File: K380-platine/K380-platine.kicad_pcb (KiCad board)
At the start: 2 copper layers, 98 x 38 mm, 32 parts, among them J1 JST-PH 2, J2 Conn_01x23, J3 MicroMod-M.2E, J4 USB_C_Receptacle_USB2.0, J5 Conn_ARM_JTAG_SWD_10, Q1 PMost Enc FET -20V, Q2 Q_NMOS_DGS, SW1 EG1215AA, SW2 SW_Push, SW3 SW_Push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

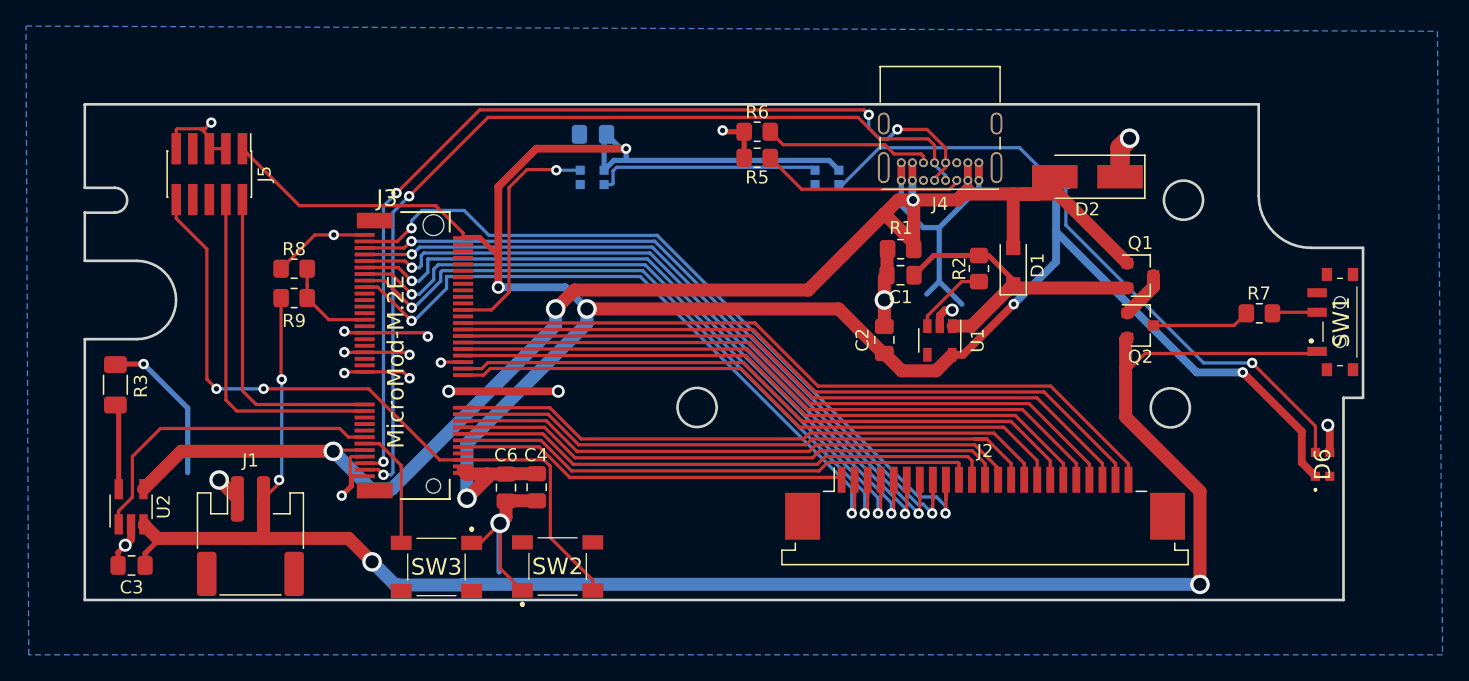
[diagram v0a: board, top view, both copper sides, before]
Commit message: Add drill mills
- needed to reroute a few tracks for it to fit
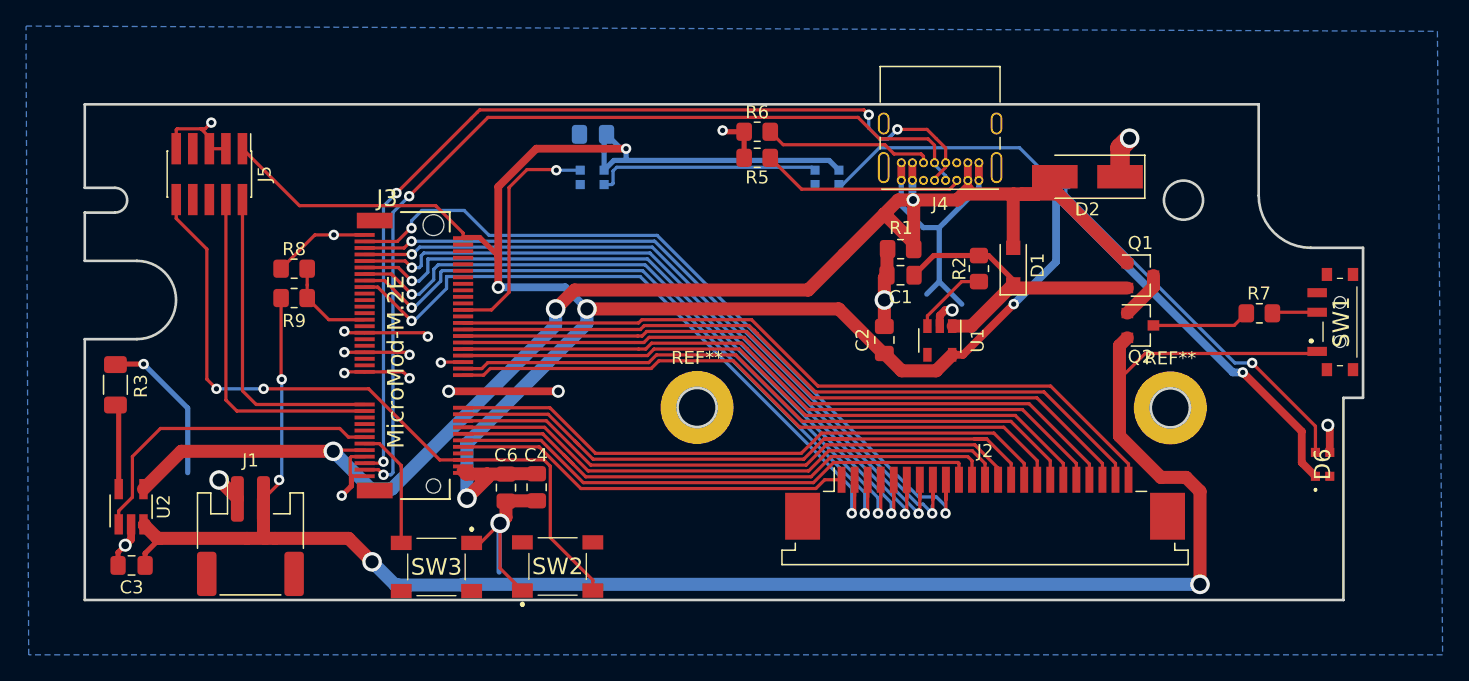
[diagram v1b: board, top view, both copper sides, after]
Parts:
- added REF**: MountingHole_3.2mm_M3_DIN965_Pad, MountingHole:MountingHole_3.2mm_M3_DIN965_Pad, F.Cu at (158.9, 85.7)
- added REF**: MountingHole_3.2mm_M3_DIN965_Pad, MountingHole:MountingHole_3.2mm_M3_DIN965_Pad, F.Cu at (122.6, 85.6)
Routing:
- net COL6: track 46.1 -> 49.3 mm
- net COL3: track 41.8 -> 43.6 mm
- net VBAT: track 143.0 -> 144.5 mm
- net Net-(D5-Pad2): track 30.6 -> 29.2 mm
- net V3.3: track 182.2 -> 183.5 mm
- net COL7: track 46.4 -> 47.3 mm
- net COL5: track 43.8 -> 44.7 mm
- net COL4: track 42.9 -> 43.7 mm
- net COL2: track 40.5 -> 41.3 mm
- net COL14: track 55.5 -> 56.2 mm
- net COL1: track 30.1 -> 30.6 mm

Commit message: Add test probes
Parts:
- added CSTAT1: T_CSTAT, TestPoint:TestPoint_Pad_D1.0mm, F.Cu at (80.5, 88.2)
- added DLED1: T_DLED, TestPoint:TestPoint_Pad_D1.0mm, F.Cu at (110.0, 68.5)
- added GND1: T_GND, TestPoint:TestPoint_Pad_D1.0mm, F.Cu at (170.2, 98.2)
- added V3.3: T_V3.3, TestPoint:TestPoint_Pad_D1.0mm, F.Cu at (147.2, 82.2)
- added VBAT1: T_VBAT, TestPoint:TestPoint_Pad_D1.0mm, F.Cu at (95.0, 95.5)
- added VUSB1: T_VUSB, TestPoint:TestPoint_Pad_D1.0mm, F.Cu at (127.2, 76.5)
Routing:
- net V3.3: track 183.5 -> 190.0 mm
- net DLED: track 18.2 -> 20.2 mm
- net GND: track 122.5 -> 123.9 mm, vias 21 -> 22
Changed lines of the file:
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@@
     (thickness 1.6)
     (drawings 50)
-    (tracks 627)
+    (tracks 634)
     (zones 0)
-    (modules 34)
+    (modules 40)
     (nets 71)
   )
@@
   )
   (setup
-    (last_trace_width 0.25)
+    (last_trace_width 0.4)
     (user_trace_width 0.25)
     (user_trace_width 0.4)
@@
     (add_net VBAT)
     (add_net VUSB)
+  )
+  (module TestPoint:TestPoint_Pad_D1.0mm (layer F.Cu)
+    (at 147.25 82.25)
+    (descr "SMD pad as test Point, diameter 1.0mm")
+    (tags "test point SMD pad")
+    (attr virtual)
+    (fp_text reference V3.3 (at 0 -1.448) (layer F.SilkS)
+      (effects (font (size 1 1) (thickness 0.15)))
+    )
+    (fp_text value T_V3.3 (at 0 1.55) (layer F.Fab)
+      (effects (font (size 1 1) (thickness 0.15)))
+    )
+    (fp_text user %R (at 0 -1.45) (layer F.Fab)
+      (effects (font (size 1 1) (thickness 0.15)))
+    )
+    (fp_circle (center 0 0) (end 1 0) (layer F.CrtYd) (width 0.05))
+    (fp_circle (center 0 0) (end 0 0.7) (layer F.SilkS) (width 0.12))
+    (pad 1 smd circle (at 0 0) (size 1 1) (layers F.Cu F.Mask)
+      (net 20 V3.3))
+  )
+  (module TestPoint:TestPoint_Pad_D1.0mm (layer F.Cu)
+    (at 127.25 76.5)
+    (descr "SMD pad as test Point, diameter 1.0mm")
+    (tags "test point SMD pad")
+    (attr virtual)
+    (fp_text reference VUSB1 (at 0 -1.448) (layer F.SilkS)
+      (effects (font (size 1 1) (thickness 0.15)))
+    )
+    (fp_text value T_VUSB (at 0 1.55) (layer F.Fab)
+      (effects (font (size 1 1) (thickness 0.15)))
+    )
+    (fp_text user %R (at 0 -1.45) (layer F.Fab)
+      (effects (font (size 1 1) (thickness 0.15)))
+    )
+    (fp_circle (center 0 0) (end 1 0) (layer F.CrtYd) (width 0.05))
+    (fp_circle (center 0 0) (end 0 0.7) (layer F.SilkS) (width 0.12))
+    (pad 1 smd circle (at 0 0) (size 1 1) (layers F.Cu F.Mask)
+      (net 22 VUSB))
+  )
+  (module TestPoint:TestPoint_Pad_D1.0mm (layer F.Cu)
+    (at 170.25 98.25)
+    (descr "SMD pad as test Point, diameter 1.0mm")
+    (tags "test point SMD pad")
+    (attr virtual)
+    (fp_text reference GND1 (at 0 -1.448) (layer F.SilkS)
+      (effects (font (size 1 1) (thickness 0.15)))
+    )
+    (fp_text value T_GND (at 0 1.55) (layer F.Fab)
+      (effects (font (size 1 1) (thickness 0.15)))
+    )
+    (fp_text user %R (at 0 -1.45) (layer F.Fab)
+      (effects (font (size 1 1) (thickness 0.15)))
+    )
+    (fp_circle (center 0 0) (end 1 0) (layer F.CrtYd) (width 0.05))
+    (fp_circle (center 0 0) (end 0 0.7) (layer F.SilkS) (width 0.12))
+    (pad 1 smd circle (at 0 0) (size 1 1) (layers F.Cu F.Mask)
+      (net 18 GND))
+  )
+  (module TestPoint:TestPoint_Pad_D1.0mm (layer F.Cu)
+    (at 80.5 88.25)
+    (descr "SMD pad as test Point, diameter 1.0mm")
+    (tags "test point SMD pad")
+    (attr virtual)
+    (fp_text reference CSTAT1 (at 0 -1.448) (layer F.SilkS)
+      (effects (font (size 1 1) (thickness 0.15)))
+    )
+    (fp_text value T_CSTAT (at 0 1.55) (layer F.Fab)
+      (effects (font (size 1 1) (thickness 0.15)))
+    )
+    (fp_text user %R (at 0 -1.45) (layer F.Fab)
+      (effects (font (size 1 1) (thickness 0.15)))
+    )
+    (fp_circle (center 0 0) (end 1 0) (layer F.CrtYd) (width 0.05))
+    (fp_circle (center 0 0) (end 0 0.7) (layer F.SilkS) (width 0.12))
+    (pad 1 smd circle (at 0 0) (size 1 1) (layers F.Cu F.Mask)
+      (net 54 CSTAT))
+  )
+  (module TestPoint:TestPoint_Pad_D1.0mm (layer F.Cu)
+    (at 95 95.5 180)
+    (descr "SMD pad as test Point, diameter 1.0mm")
+    (tags "test point SMD pad")
+    (attr virtual)
+    (fp_text reference VBAT1 (at 0 -1.448) (layer F.SilkS)
+      (effects (font (size 1 1) (thickness 0.15)))
+    )
+    (fp_text value T_VBAT (at 0 1.55) (layer F.Fab)
+      (effects (font (size 1 1) (thickness 0.15)))
+    )
+    (fp_text user %R (at 0 -1.45) (layer F.Fab)
+      (effects (font (size 1 1) (thickness 0.15)))
+    )
+    (fp_circle (center 0 0) (end 1 0) (layer F.CrtYd) (width 0.05))
+    (fp_circle (center 0 0) (end 0 0.7) (layer F.SilkS) (width 0.12))
+    (pad 1 smd circle (at 0 0 180) (size 1 1) (layers F.Cu F.Mask)
+      (net 21 VBAT))
+  )
+  (module TestPoint:TestPoint_Pad_D1.0mm (layer F.Cu)
+    (at 110 68.5 180)
+    (descr "SMD pad as test Point, diameter 1.0mm")
+    (tags "test point SMD pad")
+    (attr virtual)
+    (fp_text reference DLED1 (at 0 -1.448) (layer F.SilkS)
+      (effects (font (size 1 1) (thickness 0.15)))
+    )
+    (fp_text value T_DLED (at 0 1.55) (layer F.Fab)
+      (effects (font (size 1 1) (thickness 0.15)))
+    )
+    (fp_text user %R (at 0 -1.45) (layer F.Fab)
+      (effects (font (size 1 1) (thickness 0.15)))
+    )
+    (fp_circle (center 0 0) (end 1 0) (layer F.CrtYd) (width 0.05))
+    (fp_circle (center 0 0) (end 0 0.7) (layer F.SilkS) (width 0.12))
+    (pad 1 smd circle (at 0 0 180) (size 1 1) (layers F.Cu F.Mask)
+      (net 23 DLED))
   )
   (module MountingHole:MountingHole_3.2mm_M3_DIN965_Pad (layer F.Cu)
@@
   (segment (start 138.3 68.23) (end 138.3 66.88) (width 0.6) (layer F.Cu) (net 18))
   (segment (start 144.25 68.23) (end 144.25 66.88) (width 0.6) (layer F.Cu) (net 18))
+  (via (at 171.25 99.25) (size 0.8) (drill 0.4) (layers F.Cu B.Cu) (net 18))
+  (segment (start 170.25 98.25) (end 171.25 99.25) (width 0.4) (layer F.Cu) (net 18))
   (segment (start 143.68 79.4) (end 142.2 79.4) (width 0.4) (layer F.Cu) (net 19))
   (segment (start 147.16 76.48) (end 146.88 76.2) (width 1) (layer F.Cu) (net 19))
@@
   (segment (start 163.714998 82.95) (end 150.064999 69.300001) (width 0.6) (layer B.Cu) (net 20))
   (segment (start 164.47801 82.95) (end 163.714998 82.95) (width 0.6) (layer B.Cu) (net 20))
+  (segment (start 146.669999 82.830001) (end 147.25 82.25) (width 0.4) (layer F.Cu) (net 20))
+  (segment (start 140.969999 82.830001) (end 146.669999 82.830001) (width 0.4) (layer F.Cu) (net 20))
   (segment (start 155.5 83) (end 157 81.5) (width 0.25) (layer F.Cu) (net 21))
   (segment (start 170.02 81.5) (end 170.18 81.34) (width 0.25) (layer F.Cu) (net 21))
@@
   (segment (start 111.8 67.4) (end 111.85 67.45) (width 0.25) (layer F.Cu) (net 23))
   (segment (start 108.225001 68.774999) (end 109.6 67.4) (width 0.25) (layer F.Cu) (net 23))
-  (segment (start 108.225001 76.821031) (end 108.225001 68.774999) (width 0.25) (layer F.Cu) (net 23))
   (segment (start 106.886032 78.16) (end 108.225001 76.821031) (width 0.25) (layer F.Cu) (net 23))
   (segment (start 109.6 67.4) (end 111.8 67.4) (width 0.25) (layer F.Cu) (net 23))
   (segment (start 104.705 78.16) (end 106.886032 78.16) (width 0.25) (layer F.Cu) (net 23))
+  (segment (start 109.475001 69.024999) (end 110 68.5) (width 0.25) (layer F.Cu) (net 23))
+  (segment (start 108.225001 69.024999) (end 109.475001 69.024999) (width 0.25) (layer F.Cu) (net 23))
+  (segment (start 108.225001 76.821031) (end 108.225001 69.024999) (width 0.25) (layer F.Cu) (net 23))
+  (segment (start 108.225001 69.024999) (end 108.225001 68.774999) (width 0.25) (layer F.Cu) (net 23))
   (segment (start 116.115 68.55) (end 116.2 68.465) (width 0.25) (layer B.Cu) (net 24))
   (segment (start 115.515 68.55) (end 116.115 68.55) (width 0.25) (layer B.Cu) (net 24))
